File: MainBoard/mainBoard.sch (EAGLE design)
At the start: 103 parts, among them IC2 74HC238, IC3 74HC151D, J1 22-05-7038-03, J2 22-05-7038-03, J3 22-05-7038-03, J4 22-05-7038-03, J5 22-05-7038-03, J6 22-05-7038-03, J7 22-05-7038-03, J8 22-05-7038-03, Q1 BC847ASMD, Q10 BC847ASMD, Q2 BC847ASMD, Q5 BC847ASMD, Q6 BC847ASMD, Q9 BC847ASMD, U1 STM32F0DISCOVERY, X1 PWR12, X2 MSTBA2, X3 MSTBA2, X4 MSTBA2, X5 MSTBA2, X6 MSTBA2, X7 MSTBA2

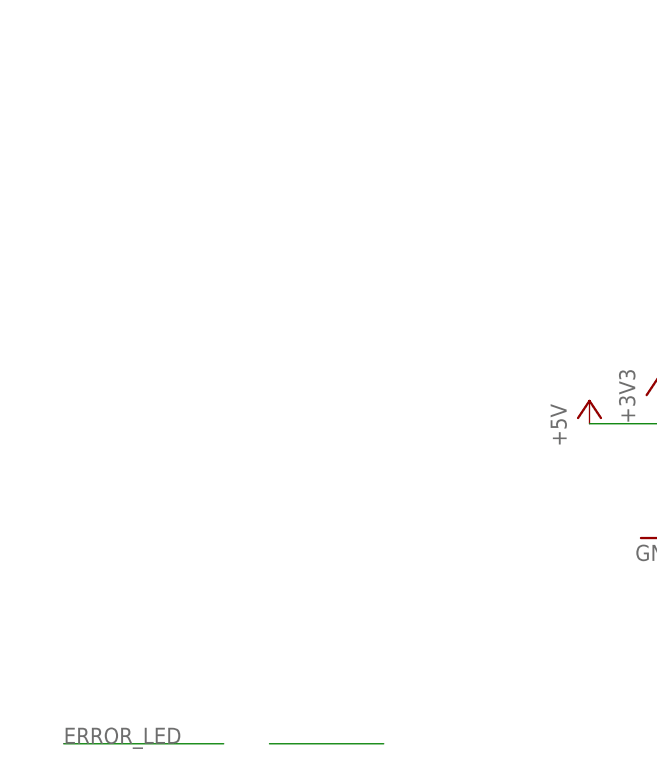
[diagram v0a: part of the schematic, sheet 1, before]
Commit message: board STM32 update
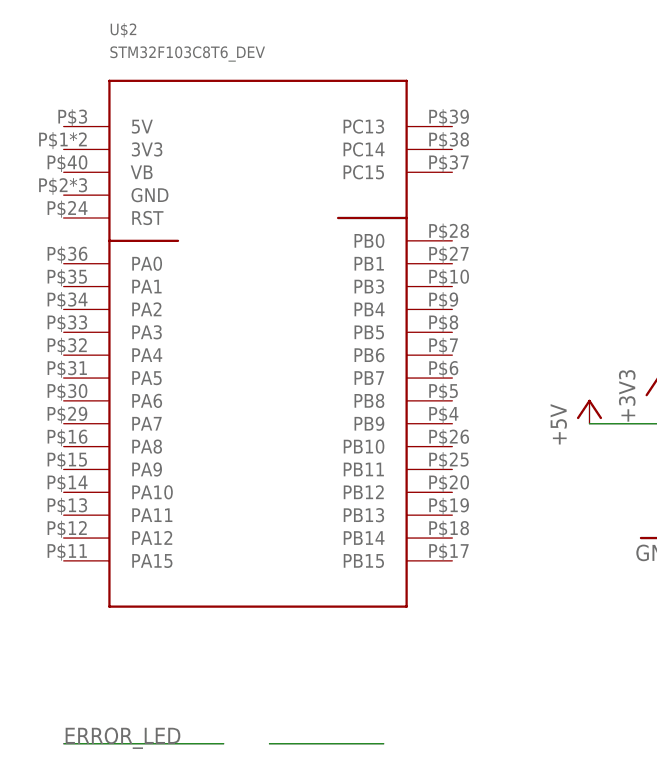
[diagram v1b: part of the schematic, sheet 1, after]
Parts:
- removed U$10, U$11: Kontakte (20Stk), extra:DUMMY_BOM
- removed U$12, U$13, U$14, U$15, U$16, U$17: AKL 249-02, extra:DUMMY_BOM
- removed U$3, U$4, U$5, U$6, U$7, U$8, U$9: PSK 254/3W, extra:DUMMY_BOM
- U$2: value PSK 254/3W -> STM32F103C8T6_DEV; device extra:DUMMY_BOM -> extra:STM32F103C8T6_DEV; BOM yes -> (none); R PSK 254/3W -> (none)
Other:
- note added: "AKL 249-02"
- note added: "PSK 254/3W"
- note added: "PSK-KONTAKTE"

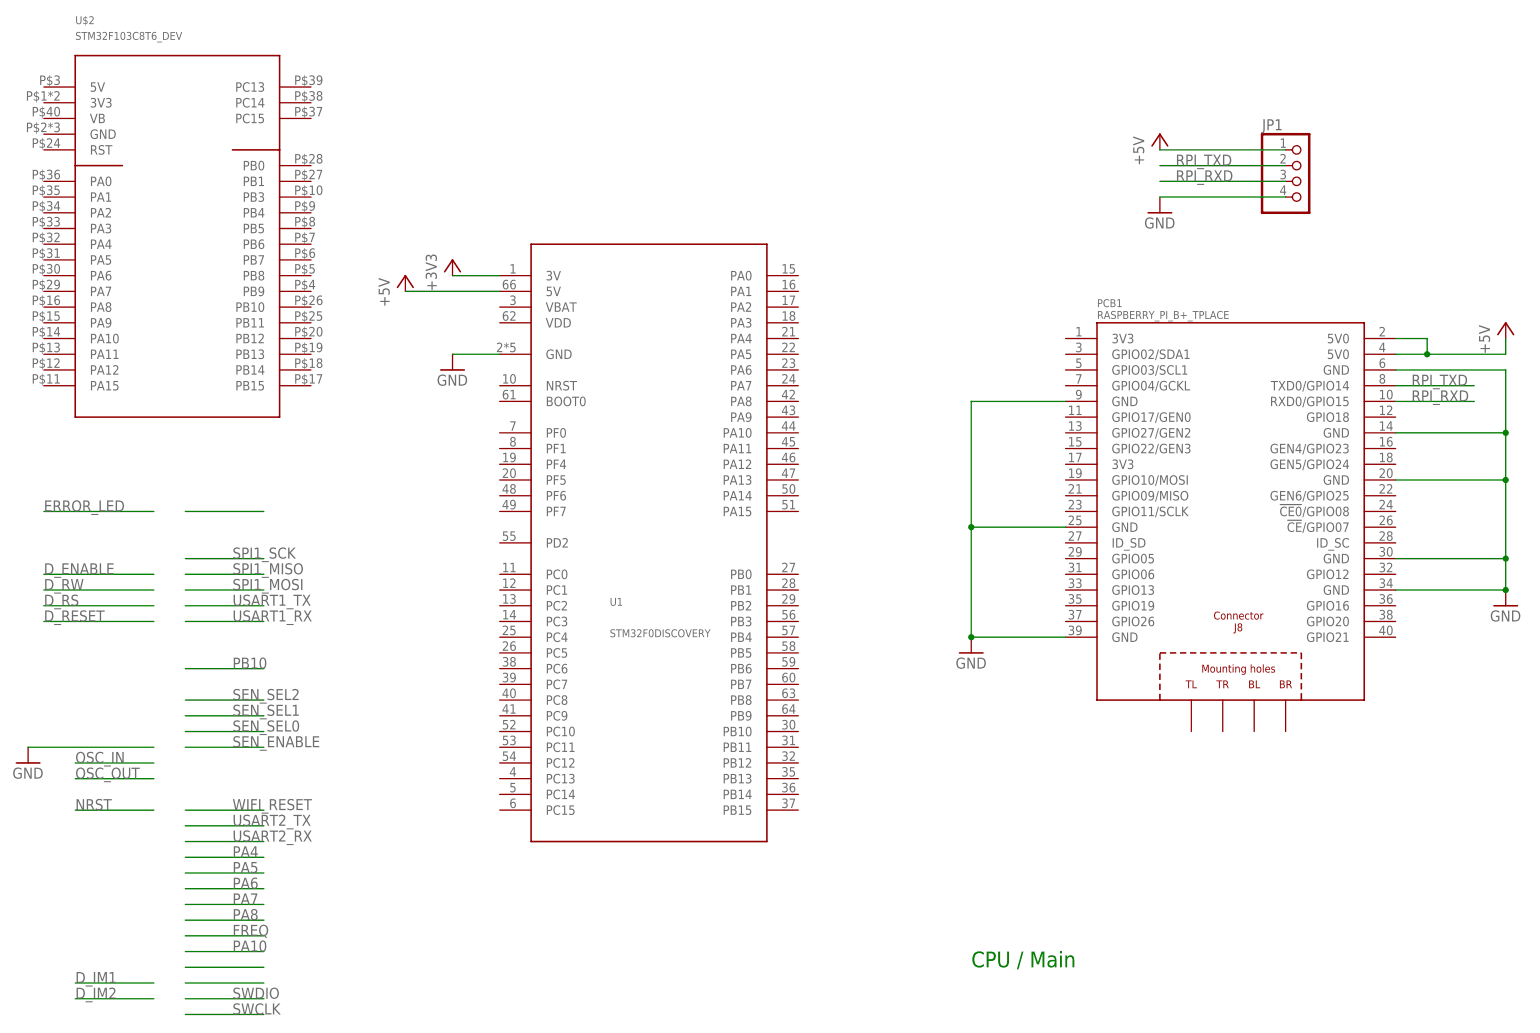
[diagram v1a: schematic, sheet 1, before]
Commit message: board updates, rpi and stm32
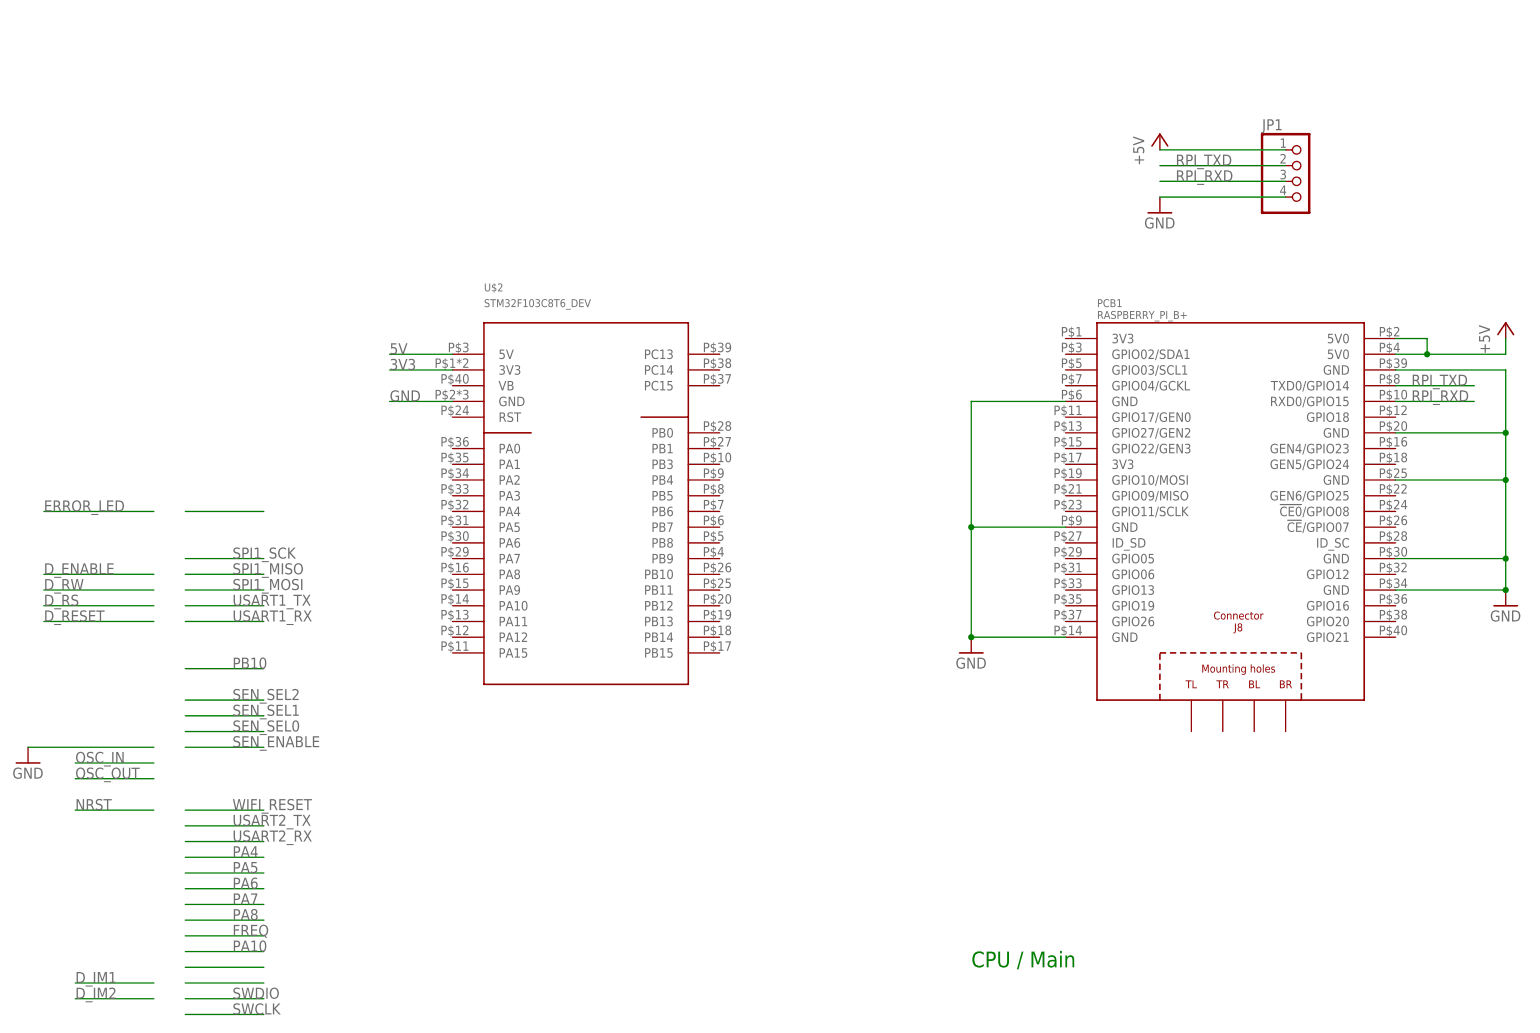
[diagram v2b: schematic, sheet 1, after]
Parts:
- removed U1: STM32F0DISCOVERY, extra:STM32F0DISCOVERY
- PCB1: value RASPBERRY_PI_B+_TPLACE -> RASPBERRY_PI_B+; device RASPBERRY_PI_Bplus:RASPBERRY_PI_B+_TPLACE -> RASPBERRY_PI_Bplus:RASPBERRY_PI_B+
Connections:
- new net 3V3: U$2.3V3
- new net 5V: U$2.5V
- net +3V3: no longer U1.3V
- net +5V: no longer U1.5V
- net GND: now also U$2.GND; no longer U1.GND
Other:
- moved on the sheet: U$2

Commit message: board updates
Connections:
- new net N$23: PCB1.3V3@1
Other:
- note added: "Buy on eBay: STM32F103C8T6"
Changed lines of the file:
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@@
 <plain>
 <text x="162.56" y="20.32" size="2.54" layer="91">CPU / Main</text>
+<text x="81.28" y="63.5" size="1.778" layer="91">Buy on eBay: STM32F103C8T6</text>
 </plain>
 <instances>
@@
 </segment>
 </net>
+<net name="N$23" class="0">
+<segment>
+<pinref part="PCB1" gate="G$1" pin="3V3@1"/>
+<wire x1="177.8" y1="121.92" x2="162.56" y2="121.92" width="0.1524" layer="91"/>
+</segment>
+</net>

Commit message: board updates
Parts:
- added JP2: UART_STM, pinhead:PINHD-1X3
- JP1: value (none) -> UART_RPI; device pinhead:PINHD-1X4 -> pinhead:PINHD-1X3
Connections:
- removed net 5V: U$2.5V
- removed net ERROR_LED: LED2.A
- removed net N$23: PCB1.3V3@1
- new net LED_ERR: LED2.A, U$2.PB9
- new net N$30: PCB1.GND@8
- new net SPI1_MISO: PCB1.GPIO09/MISO, U$2.PA6/SPI1_MISO
- new net SPI1_MOSI: PCB1.GPIO10/MOSI, U$2.PA7/SPI1_MOSI
- new net SPI1_SCK: PCB1.GPIO11/SCLK, U$2.PA5/SPI1_SCK
- new net STM_RXD: JP2.2, U$2.PA10/USART1_RX
- new net STM_TXD: JP2.1, U$2.PA9/USART1_TX
- net +5V: now also U$2.5V; no longer JP1.1
- net GND: now also JP1.3, JP2.3; no longer JP1.4, PCB1.GND@8
- net RPI_RXD: now also JP1.2; no longer JP1.3
- net RPI_TXD: now also JP1.1; no longer JP1.2
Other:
- note removed: "User Interface"

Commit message: mainboard updates
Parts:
- added IC1: 74HC238, 74xx-eu:74HC138D
- R3: value 100 -> 150
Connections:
- net SEN_SEL0 renamed SEN_A0
- net SEN_SEL1 renamed SEN_A1
- net SEN_SEL2 renamed SEN_A2
- removed net +3V3: R4.2
- removed net PA4: R7.1
- removed net PA6: R15.1
- removed net PA7: R23.1
- removed net PA8: R24.1
- removed net PB0: R8.1
- removed net PB10: R16.1
- new net N$24: IC2A.G2A, IC2A.G2B
- new net PWM: IC1A.G1, U$2.PA1
- new net PWM_A0: IC1A.A, U$2.PC14
- new net PWM_A1: IC1A.B, U$2.PC15
- new net PWM_A2: IC1A.C, U$2.PA0
- new net RPI_NRST: PCB1.RST_RUN, U$2.PC13
- new net WP1C: IC1A.Y0, R7.1
- new net WP2C: IC1A.Y1, R15.1
- new net WP3C: IC1A.Y2, R23.1
- new net WP4C: IC1A.Y4, R8.1
- new net WP5C: IC1A.Y3, R16.1
- new net WP6C: IC1A.Y5, R24.1
- net +5V: no longer IC2A.G1
- net GND: now also IC1A.G2A, IC1A.G2B, IC3A.G, PCB1.BL, PCB1.BR, PCB1.GND@9, PCB1.TR, R4.1
- net SEN_ENABLE: now also IC2A.G1, R4.2; no longer IC2A.G2A, IC2A.G2B, IC3A.G, R4.1
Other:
- moved on the sheet: C10, C11, C12, C7, C8, C9, D2, D3, D4, D5, D6, D7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

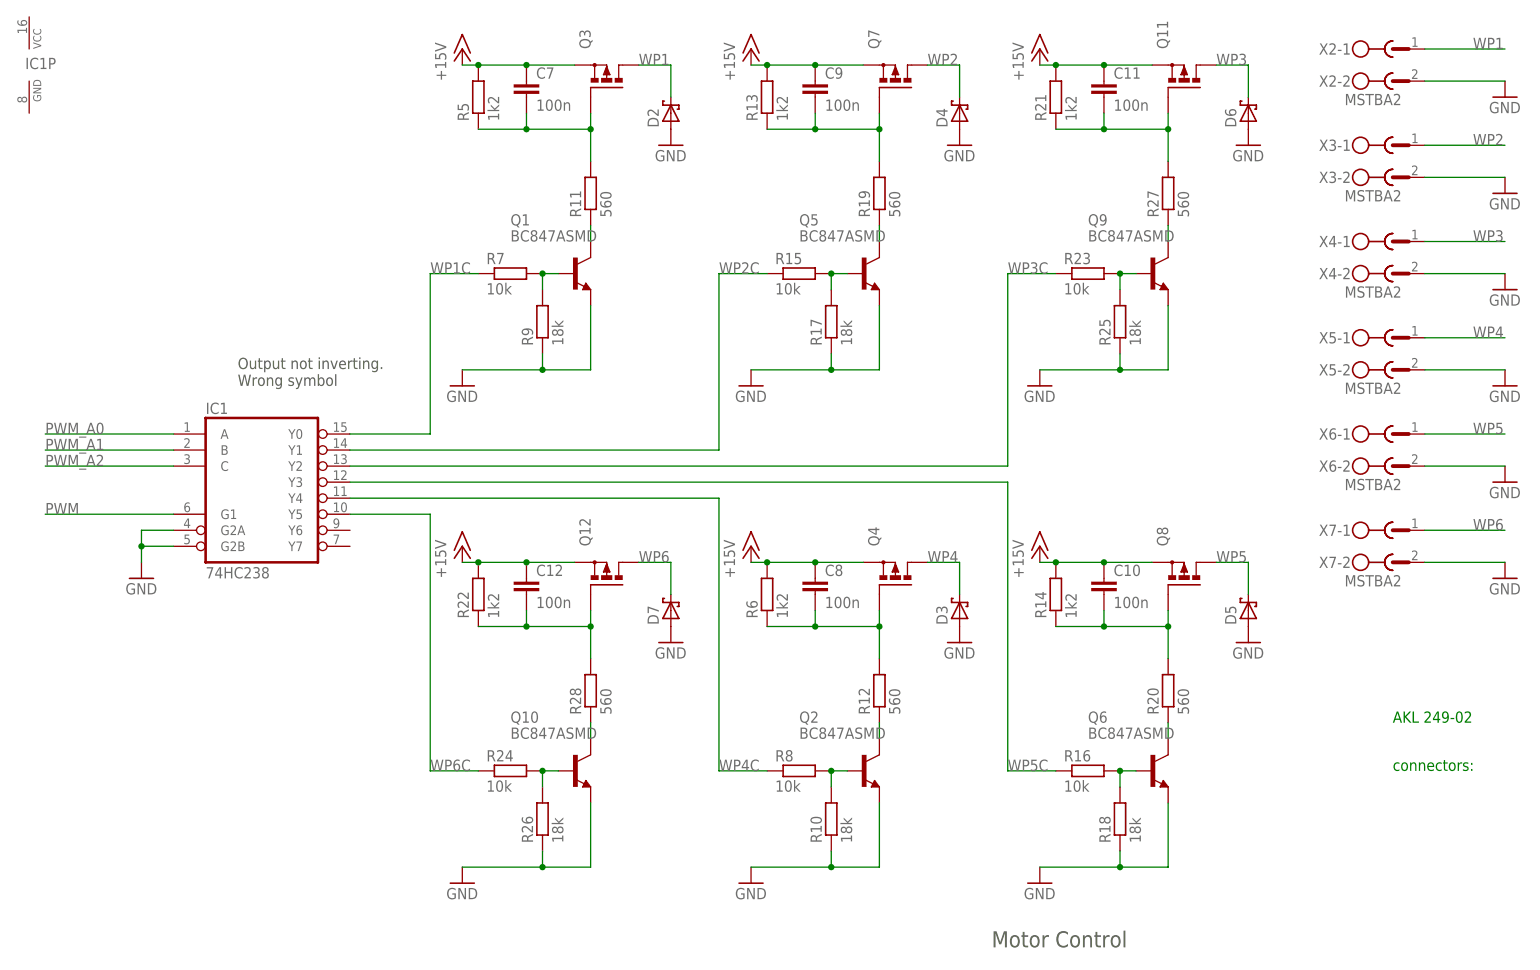
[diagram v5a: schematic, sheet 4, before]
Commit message: mainboard updates motor curcuit
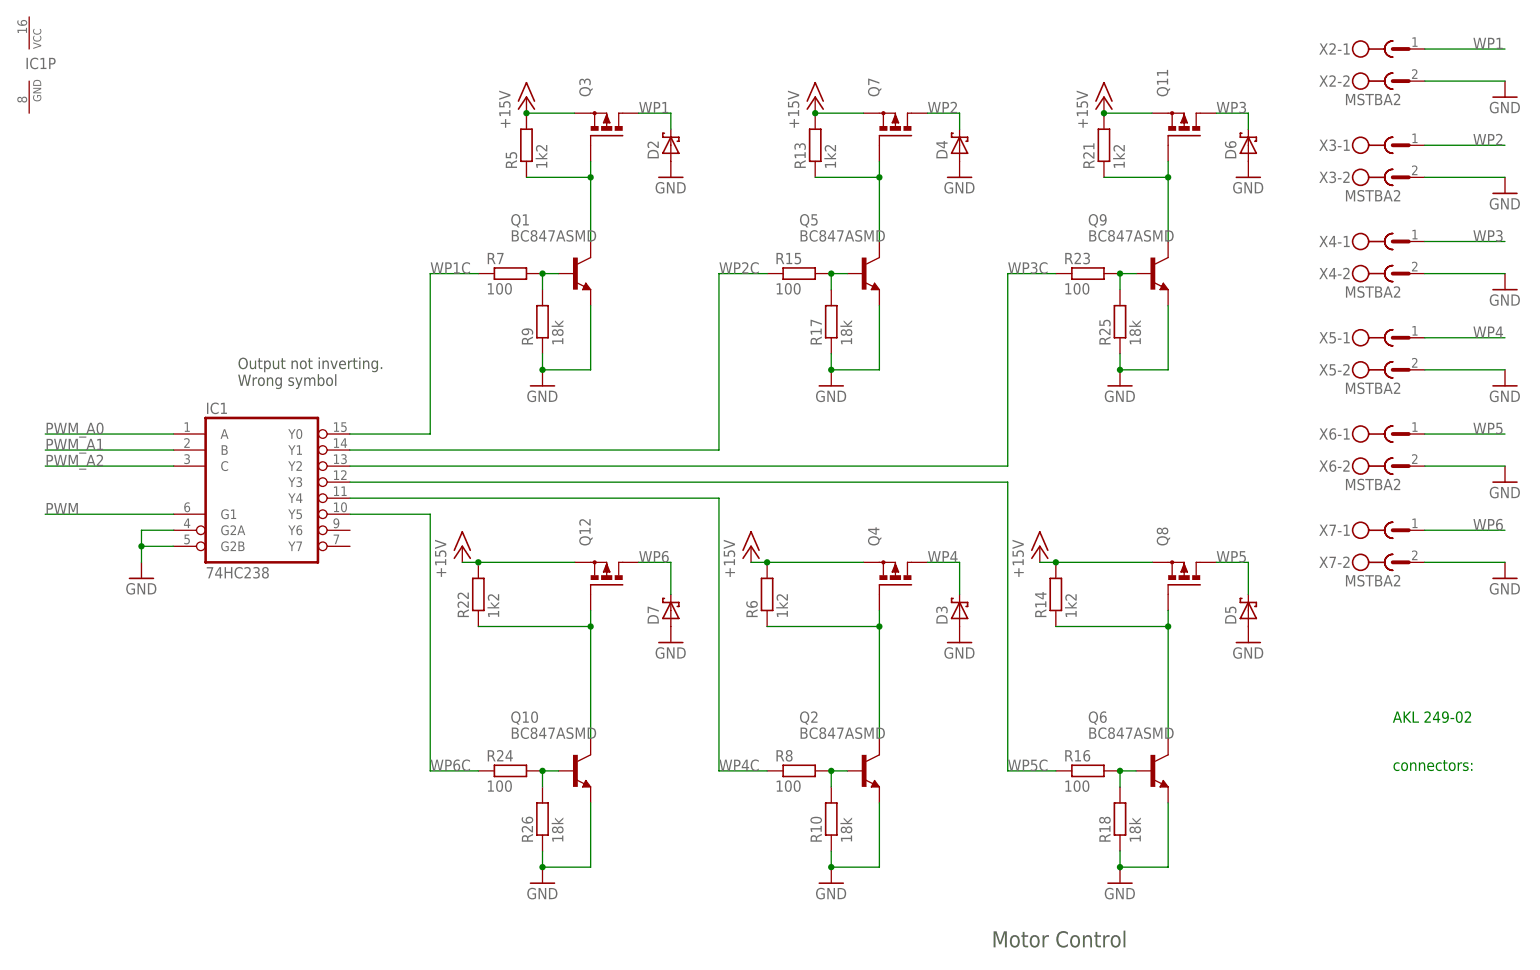
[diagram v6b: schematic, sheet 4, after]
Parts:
- removed C10, C11, C12, C7, C8, C9: 100n, rcl:C-EUC0805
- removed R11, R12, R19, R20, R27, R28: 560, rcl:R-EU_R0805
- R15, R16, R23, R24, R7, R8: value 10k -> 100; R SMD-0805 10,0K -> SMD-0805 100
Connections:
- removed net N$10: Q9.C, R27.1
- removed net N$14: Q2.C, R12.1
- removed net N$16: C10.2, Q8.G, R14.1, R20.2
- removed net N$19: C12.2, Q12.G, R22.1, R28.2
- removed net N$4: Q1.C, R11.1
- removed net N$6: Q5.C, R19.1
- net +15V: no longer C10.1, C11.1, C12.1, C7.1, C8.1, C9.1
- net N$13: now also Q2.C; no longer C8.2, R12.2
- net N$17: now also Q8.G, R14.1; no longer R20.1
- net N$2: now also Q5.C; no longer C9.2, R19.2
- net N$21: now also Q12.G, R22.1; no longer R28.1
- net N$3: now also Q1.C; no longer C7.2, R11.2
- net N$8: now also Q9.C; no longer C11.2, R27.2
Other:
- moved on the sheet: D2, D4, D6, Q11, Q3, Q7, R13, R21, R5

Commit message: mainboard updates
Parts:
- removed D5, D7: (no value), diode:SCHOTTKY-DIODESMC
- removed Q10, Q6: BC847ASMD, transistor-npn:BC847ASMD
- removed Q12, Q8: (no value), transistor-power:P-MOSFET-SO8
- removed R14, R22: 1k2, rcl:R-EU_R0805
- removed R16, R24: 100, rcl:R-EU_R0805
- removed R18, R26: 18k, rcl:R-EU_R0805
- removed X6, X7: MSTBA2, con-phoenix-508:MSTBA2
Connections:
- removed net N$17: Q6.C, Q8.G, R14.1
- removed net N$18: Q6.B, R16.2, R18.2
- removed net N$21: Q10.C, Q12.G, R22.1
- removed net N$22: Q10.B, R24.2, R26.2
- removed net WP5: D5.C, Q8.D, X6-1.1
- removed net WP5C: IC1A.Y3, R16.1
- removed net WP6: D7.C, Q12.D, X7-1.1
- removed net WP6C: IC1A.Y5, R24.1
- net +15V: no longer Q12.S, Q8.S, R14.2, R22.2
- net GND: no longer D5.A, D7.A, Q10.E, Q6.E, R18.1, R26.1, X6-2.1, X7-2.1
- net WP4C: now also IC1A.Y3; no longer IC1A.Y4

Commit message: mainboard updates
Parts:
- removed J6, J7, J8: 22-05-7038-03, con-molex:22-05-7038-03
- added D5: (no value), diode:DIODE-DO-214AC
- added Q6: BC847ASMD, transistor-npn:BC847ASMD
- added Q8: (no value), transistor-power:P-MOSFET-SO8
- added R11: 100, rcl:R-EU_R0805
- added R12: 18k, rcl:R-EU_R0805
- added R14: 1k2, rcl:R-EU_R0805
- added X6: MSTBA2, con-phoenix-508:MSTBA2
- D2, D3, D4, D6: device diode:SCHOTTKY-DIODESMC -> diode:DIODE-DO-214AC
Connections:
- removed net S6_3V: IC2A.Y5, J6-1.S
- removed net S6_DAT: IC3A.D5, J6-2.S
- removed net S7_3V: IC2A.Y6, J7-1.S
- removed net S7_DAT: IC3A.D6, J7-2.S
- removed net S8_3V: IC2A.Y7, J8-1.S
- removed net S8_DAT: IC3A.D7, J8-2.S
- new net N$4: Q6.C, Q8.G, R14.1
- new net N$6: Q6.B, R11.2, R12.2
- new net WP5: D6.C, Q8.D, X6-1.1
- new net WP5C: IC1A.Y4, R11.1
- net +15V: now also Q8.S, R14.2
- net GND: now also D5.A, Q6.E, R12.1, X6-2.1; no longer J6-3.S, J7-3.S, J8-3.S
- net WP2: now also D3.C; no longer D4.C
- net WP3: now also D4.C; no longer D6.C
- net WP4: now also D5.C; no longer D3.C
